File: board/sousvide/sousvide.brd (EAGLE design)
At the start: 91.1 x 64.8 mm, 15 parts, among them K1 G5L, Q1 BC548

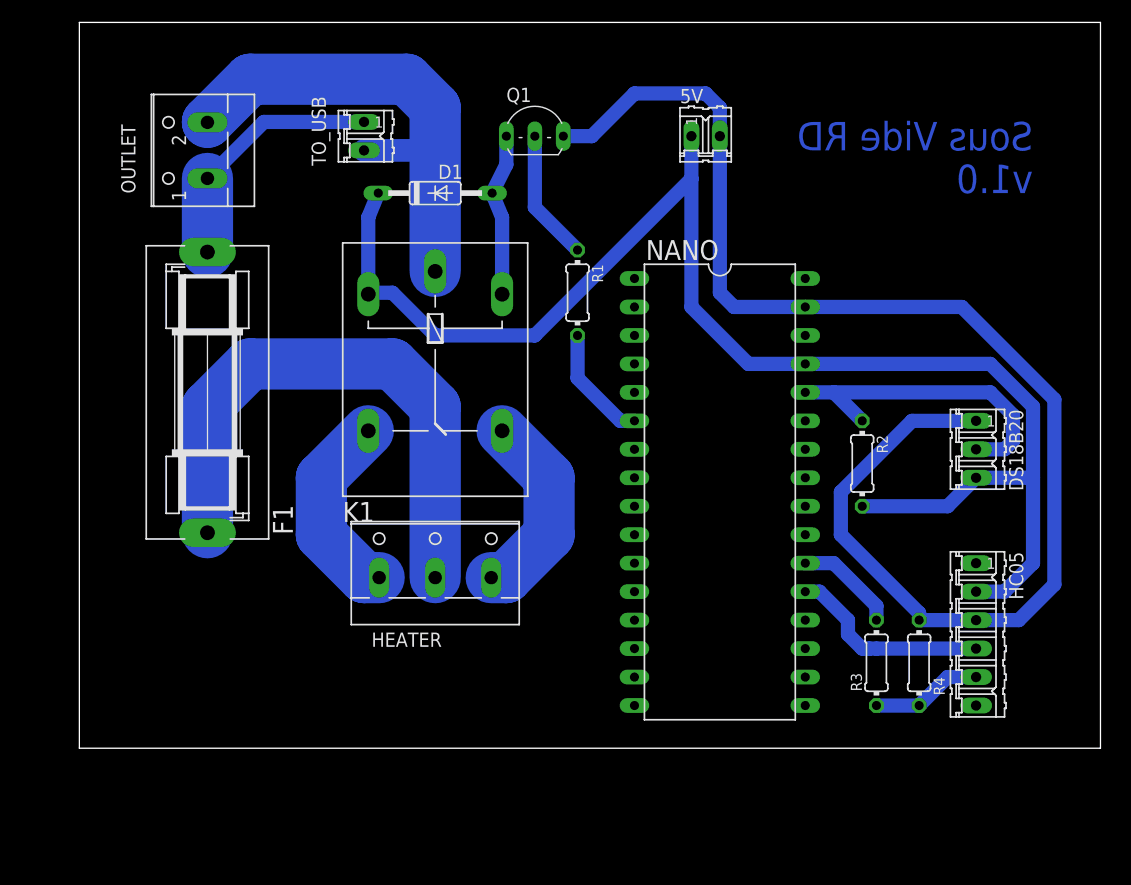
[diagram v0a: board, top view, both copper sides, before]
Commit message: Board change
Changed design so the BT module can fit over the board
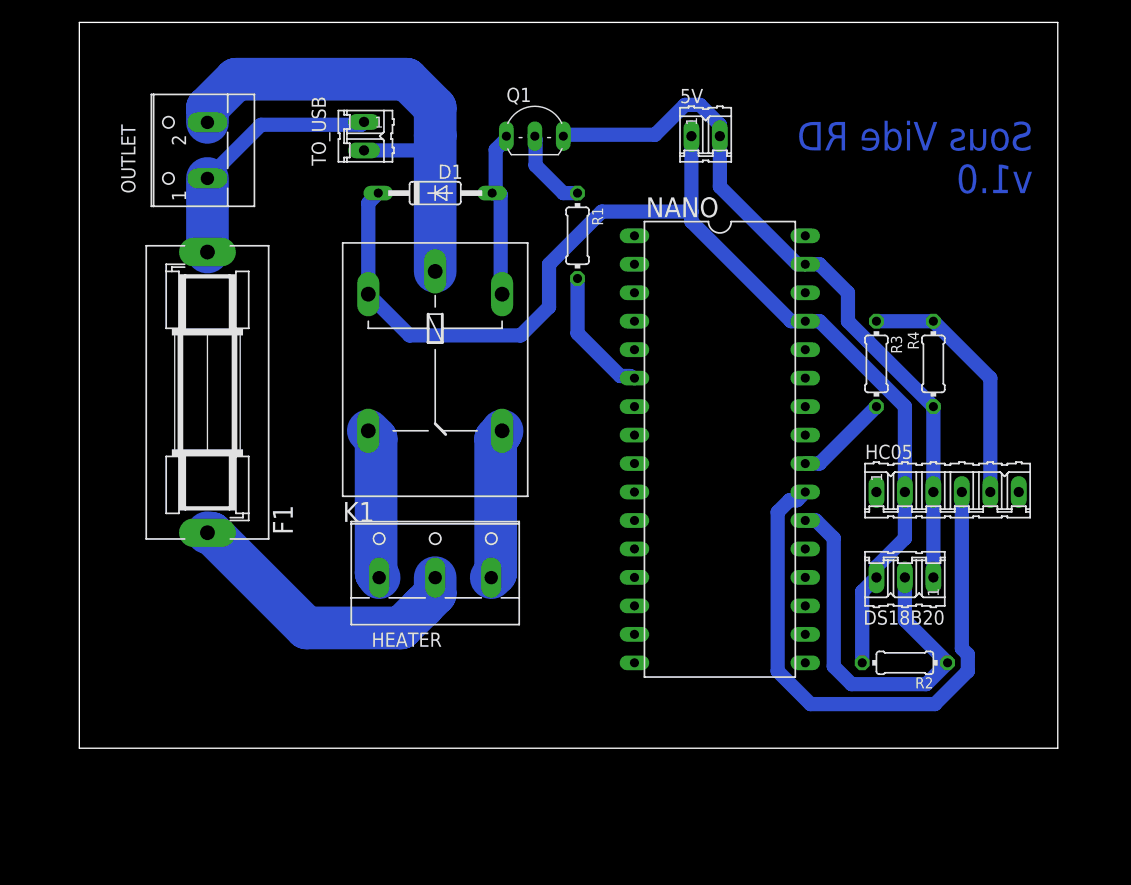
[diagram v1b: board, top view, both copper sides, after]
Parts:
- moved R4 26.7 mm to (81.3, 44.5), turned to 90 degrees
- moved R3 26.7 mm to (76.2, 44.5), turned to 270 degrees
- moved R2 18.2 mm to (78.7, 17.8), turned to 180 degrees
- moved DS18B20 13.1 mm to (78.7, 25.4), turned to 180 degrees
- moved HC05 13.0 mm to (82.5, 33.0), turned to 0 degrees
- moved R1 5.08 mm to (49.5, 55.9)
- moved NANO 3.81 mm to (62.2, 36.8)
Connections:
- net N$10 renamed BTRX
- net N$11 renamed RELAYNC
- net N$3 renamed RELAYNA
- net N$5 renamed RELAYCONTROL
- removed net N$12: NANO.22, R3.2
- removed net N$4: DS18B20.2, NANO.28, R2.1
- removed net N$9: HC05.4, NANO.21
- new net NANORX: HC05.4, NANO.23
- new net NANOTX: NANO.24, R3.2
- new net ONEWIRE: DS18B20.2, NANO.22, R2.1
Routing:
- net GND: track 125.3 -> 65.3 mm
- net NANORX: track 0.00 -> 53.0 mm
- net ONEWIRE: track 0.00 -> 35.4 mm
- net N$4: track 28.9 -> 0.00 mm
- net +5V: track 131.2 -> 104.5 mm
- net N$8: track 50.0 -> 26.5 mm
- net N$9: track 18.1 -> 0.00 mm
- net N$2: track 59.1 -> 45.2 mm
- net BTRX: track 9.94 -> 22.4 mm
- net N$12: track 9.20 -> 0.00 mm
- net NANOTX: track 0.00 -> 8.45 mm
- net N$7: track 11.7 -> 7.38 mm
- net RELAYNA: track 17.8 -> 13.5 mm
- net RELAYNC: track 17.8 -> 13.5 mm
- net RELAYCONTROL: track 10.5 -> 11.6 mm
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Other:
- board size 91.1 x 64.8 mm -> 87.3 x 64.8 mm

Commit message: New fuse
Updating fuse holder footprint to match the one we bought
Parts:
- F1: value (none) -> FUSESH22,5; device fuse:SH25 -> fuse:SH22,5
- moved R2 9.25 mm to (76.2, 26.7), turned to 0 degrees
- moved R3 5.85 mm to (80.0, 40.0), turned to 180 degrees
- moved DS18B20 5.12 mm to (78.1, 20.3)
- moved R4 2.84 mm to (80.0, 47.0), turned to 0 degrees
- moved 5V 1.91 mm to (59.1, 64.8), turned to 90 degrees
- moved F1 1.27 mm to (16.5, 43.2)
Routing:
- net ONEWIRE: track 35.4 -> 23.6 mm
- net N$8: track 26.5 -> 35.3 mm
- net BTRX: track 22.4 -> 15.0 mm
- net GND: track 65.3 -> 72.2 mm
- net +5V: track 104.5 -> 101.5 mm
- net NANORX: track 53.0 -> 55.8 mm
- net N$2: track 45.2 -> 46.9 mm

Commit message: Board corrections
Changed relay transistor to PNP, to avoid turning the heater on during reset and with the device turned off.
Changed transistor base resistor to 4k7. Old value did not allowed enough current to switch the relay.
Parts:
- Q1: value BC548 -> BC558C; device transistor-npn:TO92-EBC -> transistor-pnp:TO92-EBC
- R1: value 47k -> 4k7
- moved Q1 1.27 mm to (45.7, 64.8), turned to 180 degrees
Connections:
- net GND: now also Q1.C; no longer Q1.E
- net N$6: now also Q1.E; no longer Q1.C
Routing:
- net N$7: track 7.38 -> 8.67 mm
- net N$6: track 15.4 -> 16.7 mm
- net GND: track 72.2 -> 71.7 mm
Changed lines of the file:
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@@
 <attribute name="VALUE" x="61.341" y="53.721" size="1.778" layer="27" rot="R270"/>
 </element>
-<element name="Q1" library="transistor-npn" library_urn="urn:adsk.eagle:library:398" package="TO92-EBC" package3d_urn="urn:adsk.eagle:package:28989/2" value="BC548" x="45.72" y="66.04" smashed="yes">
-<attribute name="NAME" x="43.18" y="67.818" size="1.27" layer="25" ratio="10"/>
-<attribute name="VALUE" x="43.18" y="61.468" size="1.27" layer="27" ratio="10"/>
+<element name="Q1" library="transistor-pnp" library_urn="urn:adsk.eagle:library:399" package="TO92-EBC" package3d_urn="urn:adsk.eagle:package:29218/2" value="BC558C" x="45.72" y="64.77" smashed="yes" rot="R180">
+<attribute name="NAME" x="48.26" y="62.992" size="1.27" layer="25" ratio="10" rot="R180"/>
+<attribute name="VALUE" x="48.26" y="69.342" size="1.27" layer="27" ratio="10" rot="R180"/>
 </element>
-<element name="R1" library="rcl" library_urn="urn:adsk.eagle:library:334" package="0204/7" package3d_urn="urn:adsk.eagle:package:23498/2" value="47k" x="49.53" y="55.88" smashed="yes" rot="R270">
+<element name="R1" library="rcl" library_urn="urn:adsk.eagle:library:334" package="0204/7" package3d_urn="urn:adsk.eagle:package:23498/2" value="4k7" x="49.53" y="55.88" smashed="yes" rot="R270">
 <attribute name="NAME" x="50.8254" y="58.42" size="0.9906" layer="25" ratio="10" rot="R270"/>
 <attribute name="SPICEPREFIX" value="R" x="-12.7" y="6.35" size="1.778" layer="27" rot="R270" display="off"/>
@@
 <signal name="GND">
 <contactref element="5V" pad="2"/>
-<contactref element="Q1" pad="E"/>
+<contactref element="Q1" pad="C"/>
 <contactref element="DS18B20" pad="1"/>
 <contactref element="R4" pad="1"/>
 <contactref element="HC05" pad="3"/>
 <contactref element="NANO" pad="31"/>
-<wire x1="48.4505" y1="64.897" x2="48.26" y2="64.77" width="1.27" layer="16"/>
 <wire x1="81.28" y1="29.85539375" x2="81.28" y2="33.02" width="1.27" layer="16"/>
 <wire x1="83.7184" y1="27.41699375" x2="81.28" y2="29.85539375" width="1.27" layer="16"/>
@@
 <wire x1="81.28" y1="33.02" x2="81.28" y2="41.91" width="1.27" layer="16"/>
 <wire x1="81.28" y1="41.91" x2="76.2" y2="46.99" width="1.27" layer="16"/>
-<wire x1="59.055" y1="66.04" x2="49.5935" y2="66.04" width="1.27" layer="16"/>
-<wire x1="49.5935" y1="66.04" x2="48.4505" y2="64.897" width="1.27" layer="16"/>
 <wire x1="64.135" y1="57.15" x2="67.945" y2="53.34" width="1.27" layer="16"/>
 <wire x1="64.135" y1="57.15" x2="64.135" y2="62.865" width="1.27" layer="16"/>
@@
 <wire x1="67.945" y1="53.34" x2="69.85" y2="53.34" width="1.27" layer="16"/>
 <wire x1="72.39" y1="53.34" x2="69.85" y2="53.34" width="1.27" layer="16"/>
+<wire x1="59.055" y1="66.04" x2="48.26" y2="66.04" width="1.27" layer="16"/>
 </signal>
 <signal name="ONEWIRE">
@@
 <contactref element="Q1" pad="B"/>
 <contactref element="R1" pad="1"/>
-<wire x1="45.7835" y1="64.4525" x2="45.72" y2="64.77" width="1.27" layer="16"/>
 <wire x1="49.53" y1="59.69" x2="48.26" y2="59.69" width="1.27" layer="16"/>
-<wire x1="48.26" y1="59.69" x2="45.7835" y2="62.1665" width="1.27" layer="16"/>
-<wire x1="45.7835" y1="62.1665" x2="45.7835" y2="64.4525" width="1.27" layer="16"/>
+<wire x1="45.72" y1="62.23" x2="45.72" y2="66.04" width="1.27" layer="16"/>
+<wire x1="48.26" y1="59.69" x2="45.72" y2="62.23" width="1.27" layer="16"/>
 </signal>
 <signal name="N$6">
-<contactref element="Q1" pad="C"/>
+<contactref element="Q1" pad="E"/>
 <contactref element="K1" pad="2"/>
 <contactref element="D1" pad="A"/>
-<wire x1="42.2275" y1="63.5635" x2="42.2275" y2="60.0075" width="1.27" layer="16"/>
-<wire x1="43.1165" y1="64.4525" x2="42.2275" y2="63.5635" width="1.27" layer="16"/>
-<wire x1="42.2275" y1="60.0075" x2="41.91" y2="59.69" width="1.27" layer="16"/>
-<wire x1="43.1165" y1="64.4525" x2="43.18" y2="64.77" width="1.27" layer="16"/>
+<wire x1="41.91" y1="59.69" x2="42.2275" y2="60.0075" width="1.27" layer="16"/>
 <wire x1="42.672" y1="59.563" x2="42.672" y2="50.673" width="1.27" layer="16"/>
 <wire x1="42.672" y1="50.673" x2="42.799" y2="50.673" width="1.27" layer="16"/>
 <wire x1="42.672" y1="59.563" x2="41.91" y2="59.69" width="1.27" layer="16"/>
+<wire x1="42.2275" y1="65.0875" x2="43.18" y2="66.04" width="1.27" layer="16"/>
+<wire x1="42.2275" y1="60.0075" x2="42.2275" y2="65.0875" width="1.27" layer="16"/>
 </signal>
 <signal name="BTRX">

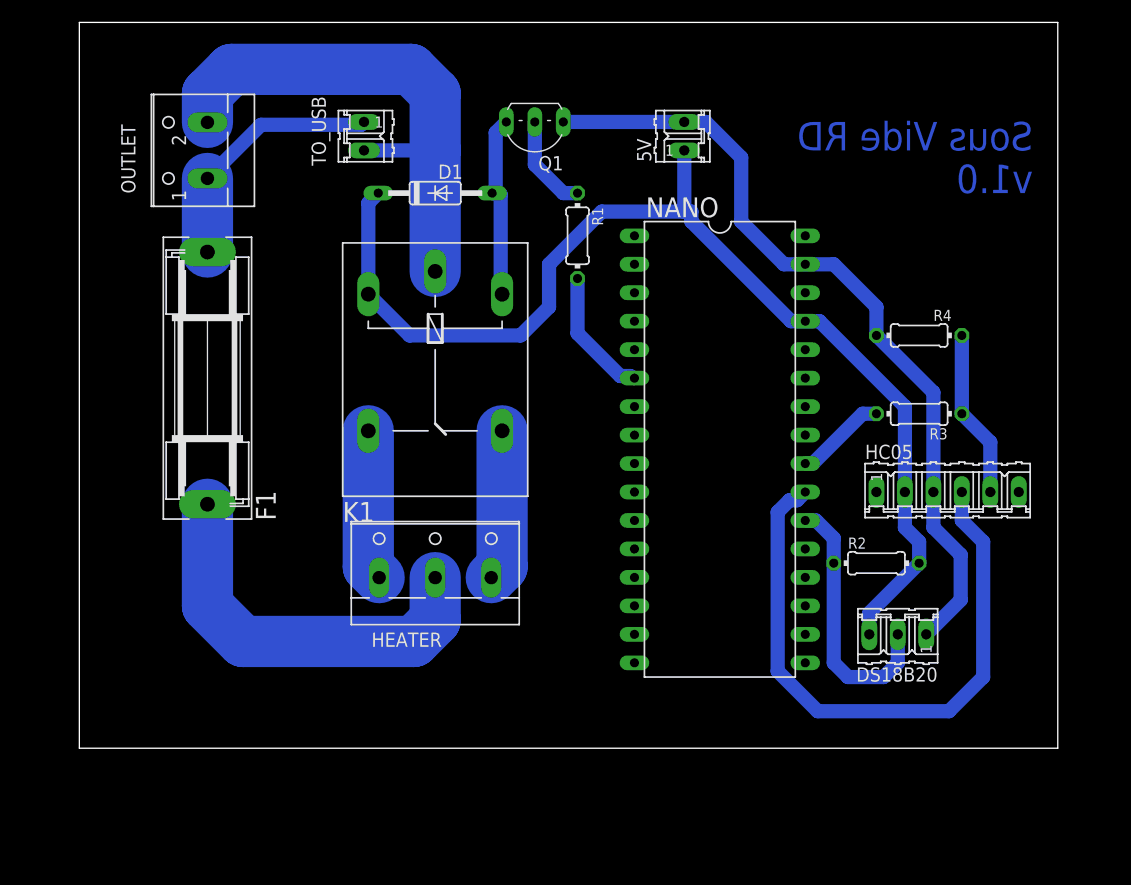
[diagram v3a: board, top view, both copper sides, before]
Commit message: Connectors update
Changing connectors to better match physical ones. Created better labels in silk layer.
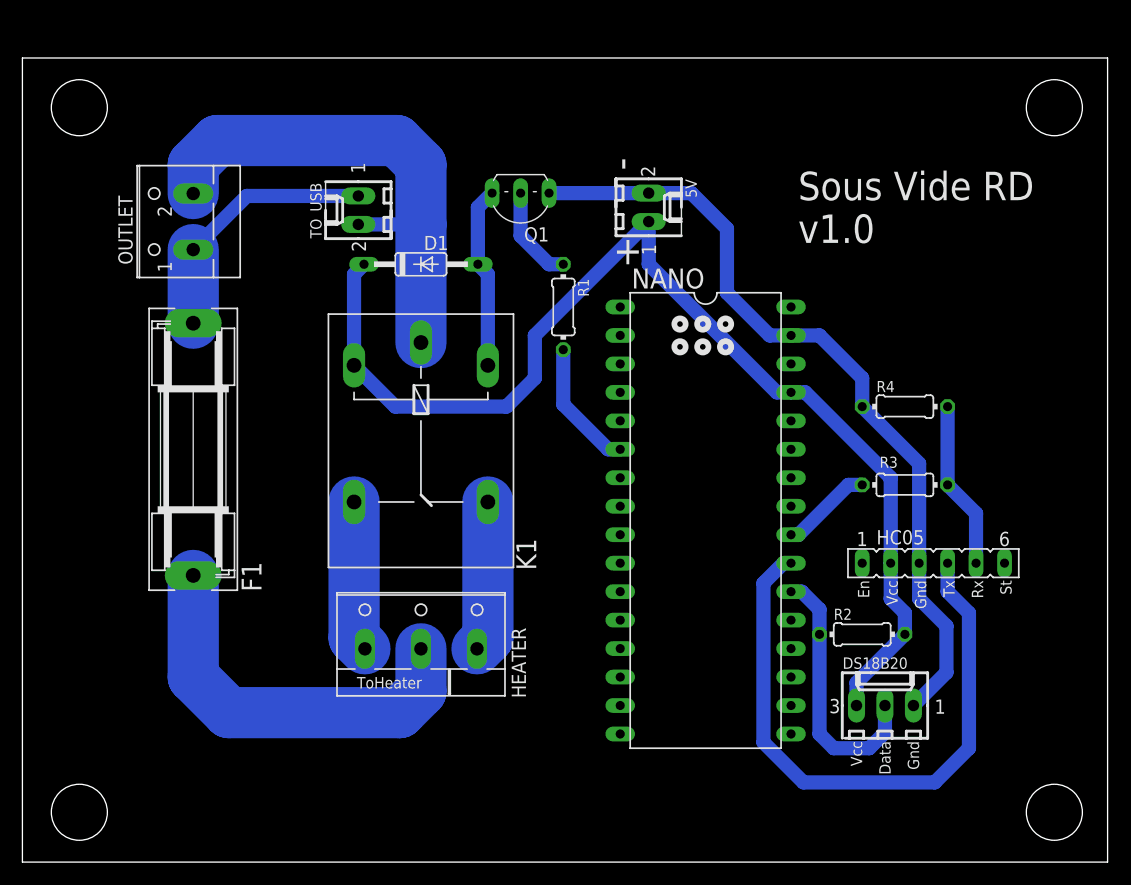
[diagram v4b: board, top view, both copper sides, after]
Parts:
- 5V, TO_USB: value (none) -> 22-27-2021-02; device con-amp-quick:02P -> con-molex:6410-02
- DS18B20: value (none) -> 22-27-2031-03; device con-amp-quick:03P -> con-molex:6410-03
- HC05: device con-amp-quick:06P -> con-lsta:FE06
- moved 5V 7.10 mm to (55.9, 58.4), turned to 270 degrees
- moved TO_USB 6.62 mm to (30.0, 58.2), turned to 90 degrees
- moved R3 6.48 mm to (78.7, 33.7)
- moved R4 6.48 mm to (78.7, 40.6)
- moved F1 6.48 mm to (15.2, 36.8)
- moved OUTLET 6.48 mm to (14.0, 57.1)
- moved R1 6.48 mm to (48.3, 49.5)
- moved HC05 6.48 mm to (81.3, 26.7)
- moved HEATER 6.48 mm to (35.6, 20.3)
- moved K1 6.48 mm to (35.6, 36.8)
- moved R2 6.48 mm to (74.9, 20.3)
- moved NANO 6.48 mm to (61.0, 30.5)
- moved D1 6.48 mm to (35.6, 53.3)
- moved Q1 6.48 mm to (44.5, 58.4)
- moved DS18B20 6.45 mm to (77.0, 14.0), turned to 0 degrees
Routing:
- net N$2: track 46.9 -> 46.1 mm
- net +5V: track 101.5 -> 102.2 mm
- net N$1: track 22.6 -> 23.3 mm
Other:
- board size 87.3 x 64.8 mm -> 96.8 x 71.7 mm
- board text added: "+"
- board text added: "-"
- board text added: "Data"
- board text added: "En"
- board text added: "Gnd"
- board text added: "Rx"
- board text added: "St"
- board text added: "ToHeater"
- board text added: "Tx"
- board text added: "Vcc"
